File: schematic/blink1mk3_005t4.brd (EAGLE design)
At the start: 15.5 x 13.7 mm, 18 parts, among them T0A TPTP15R, T1B TPTP15R, U1 EFM32HG309F64G, X1 USB

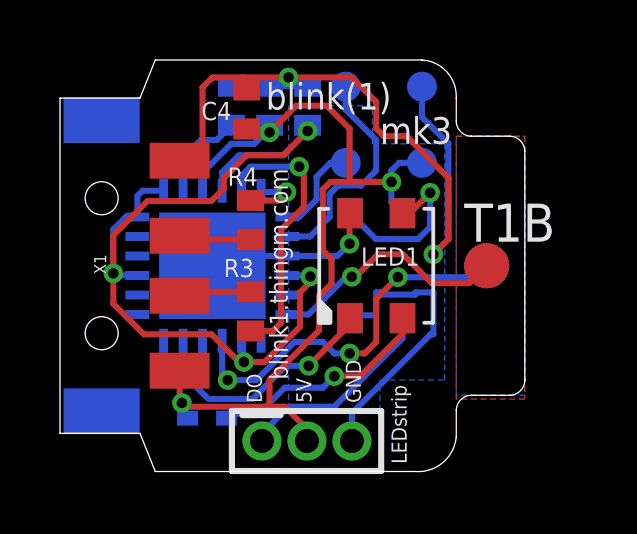
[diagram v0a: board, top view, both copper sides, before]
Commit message: small blink1 mk3 schematic fixes before release to manufacturing
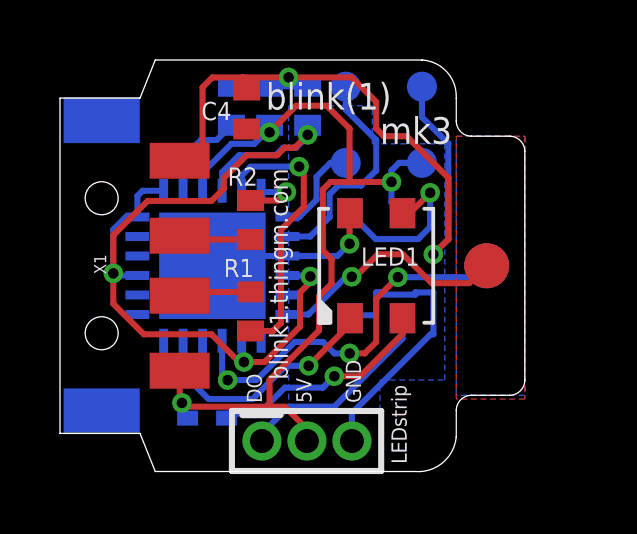
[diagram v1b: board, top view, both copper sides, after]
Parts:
- renumbered R3 to R1, R4 to R2
